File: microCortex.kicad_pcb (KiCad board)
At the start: 4 copper layers, 60.1 x 22.9 mm, 32 parts, among them J1 Feather, J2 20021121-00010C4LF, SW1 KMR231NG LFS, U1 ATSAMD21G18A-AUT, U2 BQ24075, U3 BQ27441DRZR-G1A, U4 TLV70033_WSON6, U5 BMP280, Y1 Crystal

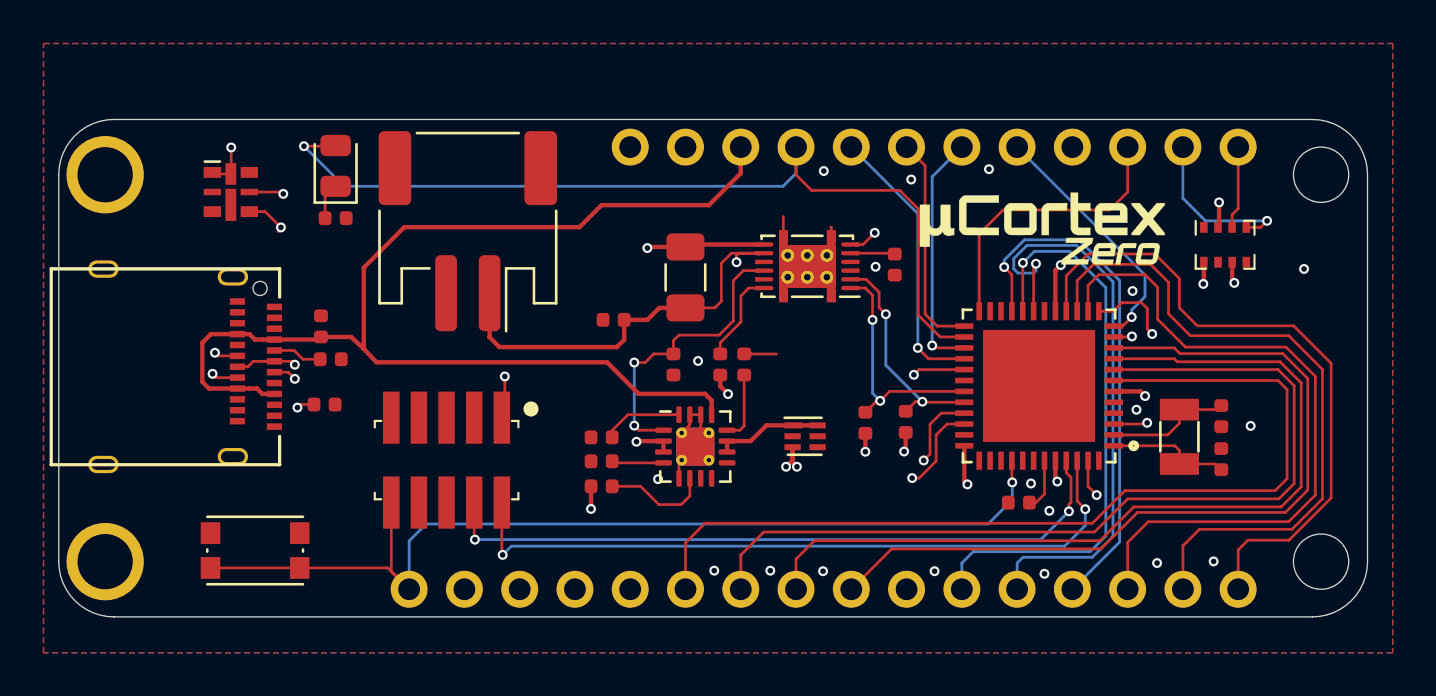
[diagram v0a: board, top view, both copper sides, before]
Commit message: Upload PDF & add pin numbers
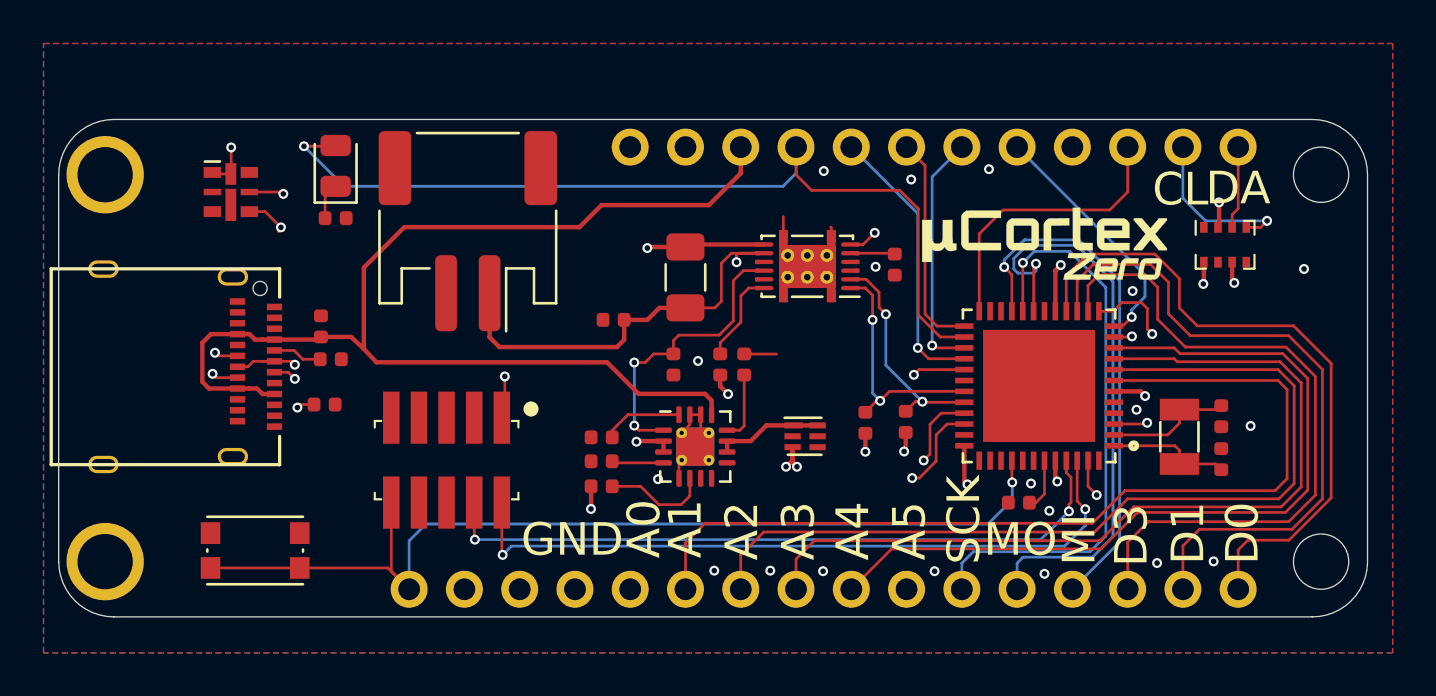
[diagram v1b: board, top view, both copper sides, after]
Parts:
- moved G*** 0.71 mm to (192.0, 97.2)
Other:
- board text added: "A0"
- board text added: "A1"
- board text added: "A2"
- board text added: "A3"
- board text added: "A4"
- board text added: "A5"
- board text added: "CL"
- board text added: "D0"
- board text added: "D1"
- board text added: "D3"
- board text added: "DA"
- board text added: "GND"
- board text added: "MI"
- board text added: "MO"
- board text added: "SCK"
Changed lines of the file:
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@@
   (general
     (thickness 1.6)
-    (drawings 4)
+    (drawings 19)
     (tracks 547)
     (zones 0)
@@
   )
   (module microCortexLogo:microCortexLogo (layer F.Cu)
-    (at 191.9 96.5)
+    (at 192 97.2)
     (fp_text reference G*** (at 0 0) (layer F.SilkS) hide
       (effects (font (size 1.524 1.524) (thickness 0.3)))
@@
     )
   )
+  (gr_text CL (at 198.25 94.7) (layer F.SilkS)
+    (effects (font (size 1.4986 1.4986) (thickness 0.29972)))
+  )
+  (gr_text DA (at 200.9 94.65) (layer F.SilkS)
+    (effects (font (size 1.4986 1.4986) (thickness 0.29972)))
+  )
+  (gr_text GND (at 170.3 110.8) (layer F.SilkS)
+    (effects (font (size 1.4986 1.4986) (thickness 0.29972)))
+  )
+  (gr_text D0 (at 201.1 110.5 90) (layer F.SilkS)
+    (effects (font (size 1.4986 1.4986) (thickness 0.29972)))
+  )
+  (gr_text D1 (at 198.6 110.5 90) (layer F.SilkS)
+    (effects (font (size 1.4986 1.4986) (thickness 0.29972)))
+  )
+  (gr_text D3 (at 196 110.6 90) (layer F.SilkS)
+    (effects (font (size 1.4986 1.4986) (thickness 0.29972)))
+  )
+  (gr_text MI (at 193.6 110.8 90) (layer F.SilkS)
+    (effects (font (size 1.4986 1.4986) (thickness 0.29972)))
+  )
+  (gr_text MO (at 190.9 110.8) (layer F.SilkS)
+    (effects (font (size 1.4986 1.4986) (thickness 0.29972)))
+  )
+  (gr_text SCK (at 188.3 109.9 90) (layer F.SilkS)
+    (effects (font (size 1.4986 1.4986) (thickness 0.29972)))
+  )
+  (gr_text A5 (at 185.8 110.4 90) (layer F.SilkS)
+    (effects (font (size 1.4986 1.4986) (thickness 0.29972)))
+  )
+  (gr_text A4 (at 183.2 110.4 90) (layer F.SilkS)
+    (effects (font (size 1.4986 1.4986) (thickness 0.29972)))
+  )
+  (gr_text A3 (at 180.7 110.4 90) (layer F.SilkS)
+    (effects (font (size 1.4986 1.4986) (thickness 0.29972)))
+  )
+  (gr_text A2 (at 178.1 110.4 90) (layer F.SilkS)
+    (effects (font (size 1.4986 1.4986) (thickness 0.29972)))
+  )
+  (gr_text A1 (at 175.5 110.3 90) (layer F.SilkS)
+    (effects (font (size 1.5 1.5) (thickness 0.3)))
+  )
+  (gr_text A0 (at 173.6 110.3 90) (layer F.SilkS)
+    (effects (font (size 1.5 1.5) (thickness 0.3)))
+  )
   (gr_circle (center 168.40416 104.7956) (end 168.60736 104.9988) (layer F.SilkS) (width 0.12))
